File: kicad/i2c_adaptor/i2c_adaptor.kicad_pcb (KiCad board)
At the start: 2 copper layers, 12 parts, among them J2 Conn_01x05, J4 Conn_01x14, J5 Conn_01x02, J6 Conn_01x14, SW1 SW_SPDT, U1 pic16f1825

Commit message: update
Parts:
- moved R1 10.2 mm to (171.4, 128.3)
- moved C1 10.2 mm to (165.1, 121.9)
- moved U1 10.2 mm to (175.3, 121.9)
- moved R2 6.48 mm to (171.4, 97.8), turned to 0 degrees
- moved R3 5.39 mm to (171.4, 100.3), turned to 0 degrees
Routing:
- net +3V3: track 177.8 -> 195.6 mm, vias 2 -> 1
- net Net-(J2-Pad5): track 7.62 -> 22.9 mm
- net Net-(J4-Pad3): track 38.1 -> 48.3 mm
- net Net-(J4-Pad10): track 33.0 -> 43.2 mm
- net Net-(J2-Pad4): track 12.7 -> 22.9 mm
- net GND: track 142.2 -> 132.1 mm, vias 0 -> 4

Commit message: update
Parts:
- removed D1: 1A, pic16f1:diode
- added Q1: Fairchild BS170, pic16f1:BS170, F.Cu at (182.9, 110.5)
- moved J5 2.54 mm to (205.7, 134.6)
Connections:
- J2 pad 2: GND -> FET
- J4 pad 1: GND -> FET
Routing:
- net GND: track 132.1 -> 71.1 mm, vias 4 -> 2
- net FET: track 0.00 -> 50.8 mm, vias 0 -> 2
- net +3V3: track 195.6 -> 167.6 mm, vias 1 -> 2
- net Net-(Q1-Pad2): track 0.00 -> 7.62 mm
- net Net-(J4-Pad3): track 48.3 -> 53.3 mm
- net Net-(J4-Pad10): track 43.2 -> 48.3 mm
- net Net-(F1-Pad1): track 5.08 -> 7.62 mm

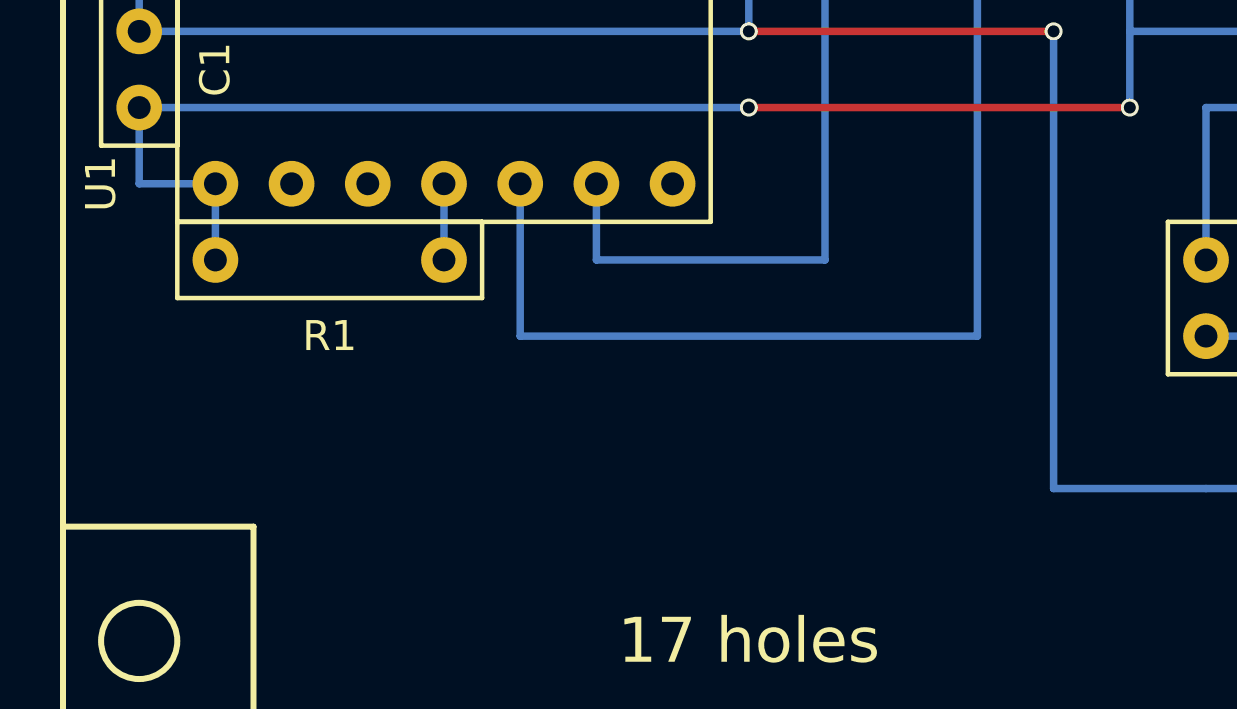
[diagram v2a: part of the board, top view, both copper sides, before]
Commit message: migration from PIC16F1825 to PIC16F18326
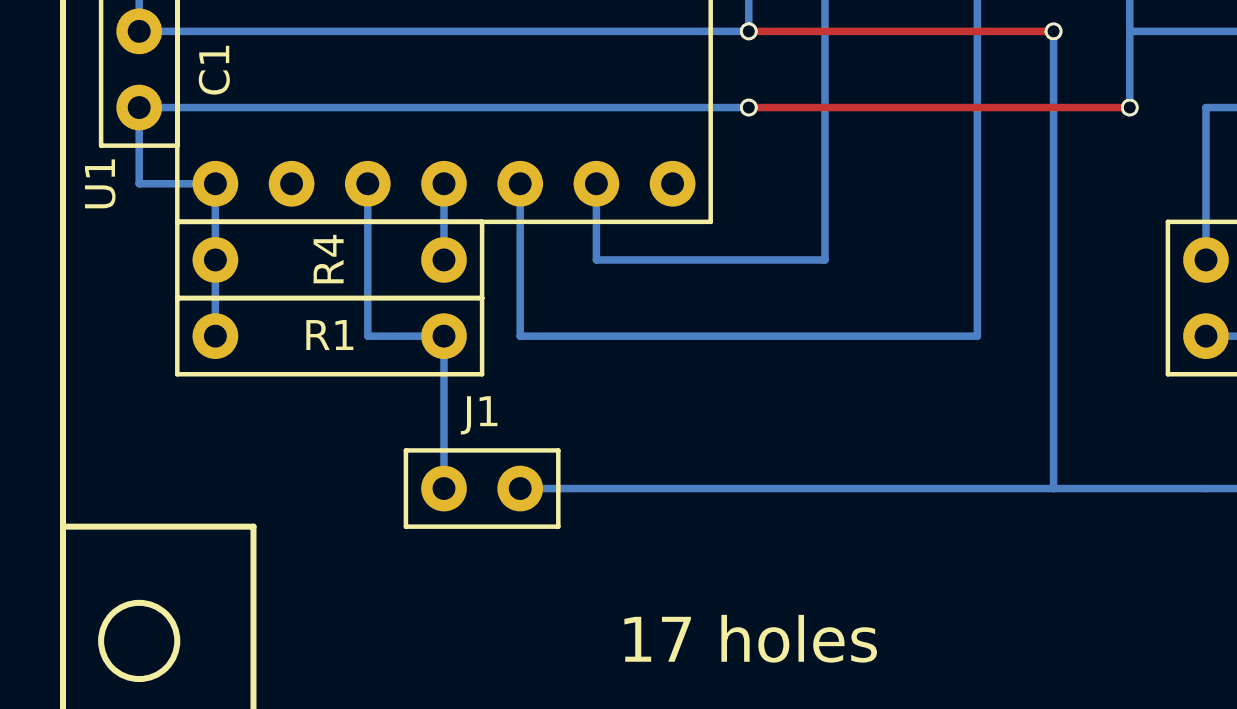
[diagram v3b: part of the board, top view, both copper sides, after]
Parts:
- added J1: Conn_01x02, mcu:Pin Header 2P, F.Cu at (176.5, 135.9)
- added R4: 51k, pic16f1:Register, F.Cu at (171.4, 130.8)
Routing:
- net GND: track 71.1 -> 88.9 mm
- net Net-(J1-Pad2): track 0.00 -> 12.7 mm
- net +3V3: track 167.6 -> 170.2 mm
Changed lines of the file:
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@@
 (kicad_pcb (version 4) (host pcbnew 4.0.7)
   (general
-    (links 26)
+    (links 30)
     (no_connects 0)
     (area 0 0 0 0)
     (thickness 1.6)
     (drawings 19)
-    (tracks 68)
+    (tracks 73)
     (zones 0)
-    (modules 12)
+    (modules 14)
     (nets 40)
   )
@@
   (net 32 "Net-(U1-Pad2)")
   (net 33 "Net-(U1-Pad13)")
-  (net 34 "Net-(U1-Pad3)")
-  (net 35 "Net-(U1-Pad12)")
-  (net 36 "Net-(U1-Pad11)")
-  (net 37 "Net-(U1-Pad7)")
-  (net 38 FET)
-  (net 39 "Net-(Q1-Pad2)")
+  (net 34 "Net-(U1-Pad12)")
+  (net 35 "Net-(U1-Pad11)")
+  (net 36 "Net-(U1-Pad7)")
+  (net 37 FET)
+  (net 38 "Net-(Q1-Pad2)")
+  (net 39 "Net-(J1-Pad2)")
   (net_class Default "This is the default net class."
     (clearance 0.2)
@@
     (add_net "Net-(F1-Pad1)")
     (add_net "Net-(F1-Pad2)")
+    (add_net "Net-(J1-Pad2)")
     (add_net "Net-(J2-Pad3)")
     (add_net "Net-(J2-Pad4)")
@@
     (add_net "Net-(U1-Pad13)")
     (add_net "Net-(U1-Pad2)")
-    (add_net "Net-(U1-Pad3)")
     (add_net "Net-(U1-Pad7)")
   )
@@
       (net 1 +3V3))
     (pad 2 thru_hole circle (at -2.54 0) (size 1.524 1.524) (drill 0.762) (layers *.Cu *.Mask)
-      (net 38 FET))
+      (net 37 FET))
     (pad 3 thru_hole circle (at 0 0) (size 1.524 1.524) (drill 0.762) (layers *.Cu *.Mask)
       (net 5 "Net-(J2-Pad3)"))
@@
     (fp_line (start -17.78 -1.27) (end -17.78 1.27) (layer F.SilkS) (width 0.15))
     (pad 1 thru_hole circle (at -16.51 0 270) (size 1.524 1.524) (drill 0.762) (layers *.Cu *.Mask)
-      (net 38 FET))
+      (net 37 FET))
     (pad 2 thru_hole circle (at -13.97 0 270) (size 1.524 1.524) (drill 0.762) (layers *.Cu *.Mask)
       (net 8 "Net-(J4-Pad2)"))
@@
       (net 33 "Net-(U1-Pad13)"))
     (pad 3 thru_hole circle (at -3.81 -2.54 90) (size 1.524 1.524) (drill 0.762) (layers *.Cu *.Mask)
-      (net 34 "Net-(U1-Pad3)"))
+      (net 39 "Net-(J1-Pad2)"))
     (pad 12 thru_hole circle (at 3.81 -2.54 90) (size 1.524 1.524) (drill 0.762) (layers *.Cu *.Mask)
-      (net 35 "Net-(U1-Pad12)"))
+      (net 34 "Net-(U1-Pad12)"))
     (pad 4 thru_hole circle (at -3.81 0 90) (size 1.524 1.524) (drill 0.762) (layers *.Cu *.Mask)
       (net 30 "Net-(R1-Pad1)"))
     (pad 11 thru_hole circle (at 3.81 0 90) (size 1.524 1.524) (drill 0.762) (layers *.Cu *.Mask)
-      (net 36 "Net-(U1-Pad11)"))
+      (net 35 "Net-(U1-Pad11)"))
     (pad 5 thru_hole circle (at -3.81 2.54 90) (size 1.524 1.524) (drill 0.762) (layers *.Cu *.Mask)
       (net 16 "Net-(J4-Pad10)"))
@@
       (net 6 "Net-(J2-Pad4)"))
     (pad 7 thru_hole circle (at -3.81 7.62 90) (size 1.524 1.524) (drill 0.762) (layers *.Cu *.Mask)
-      (net 37 "Net-(U1-Pad7)"))
+      (net 36 "Net-(U1-Pad7)"))
     (pad 8 thru_hole circle (at 3.81 7.62 90) (size 1.524 1.524) (drill 0.762) (layers *.Cu *.Mask)
-      (net 39 "Net-(Q1-Pad2)"))
+      (net 38 "Net-(Q1-Pad2)"))
   )
   (module pic16f1:Register (layer F.Cu)
@@
     (fp_line (start 3.81 -1.27) (end -3.81 -1.27) (layer F.SilkS) (width 0.15))
     (pad 1 thru_hole circle (at -2.54 0) (size 1.524 1.524) (drill 0.762) (layers *.Cu *.Mask)
-      (net 38 FET))
+      (net 37 FET))
     (pad 2 thru_hole circle (at 0 0) (size 1.524 1.524) (drill 0.762) (layers *.Cu *.Mask)
-      (net 39 "Net-(Q1-Pad2)"))
+      (net 38 "Net-(Q1-Pad2)"))
     (pad 3 thru_hole circle (at 2.54 0) (size 1.524 1.524) (drill 0.762) (layers *.Cu *.Mask)
       (net 2 GND))
+  )
+  (module "mcu:Pin Header 2P" (layer F.Cu)
+    (at 176.53 135.89 180)
+    (fp_text reference J1 (at 0 2.54 180) (layer F.SilkS)
+      (effects (font (size 1 1) (thickness 0.15)))
+    )
+    (fp_text value Conn_01x02 (at 0 -2.54 180) (layer F.Fab)
+      (effects (font (size 1 1) (thickness 0.15)))
+    )
+    (fp_line (start -2.54 -1.27) (end -2.54 1.27) (layer F.SilkS) (width 0.15))
+    (fp_line (start -2.54 1.27) (end 2.54 1.27) (layer F.SilkS) (width 0.15))
+    (fp_line (start 2.54 1.27) (end 2.54 -1.27) (layer F.SilkS) (width 0.15))
+    (fp_line (start 2.54 -1.27) (end -2.54 -1.27) (layer F.SilkS) (width 0.15))
+    (pad 1 thru_hole circle (at -1.27 0 180) (size 1.524 1.524) (drill 0.762) (layers *.Cu *.Mask)
+      (net 2 GND))
+    (pad 2 thru_hole circle (at 1.27 0 180) (size 1.524 1.524) (drill 0.762) (layers *.Cu *.Mask)
+      (net 39 "Net-(J1-Pad2)"))
+  )
+  (module pic16f1:Register (layer F.Cu)
+    (at 171.45 130.81)
+    (fp_text reference R4 (at 0 -2.54 90) (layer F.SilkS)
+      (effects (font (size 1 1) (thickness 0.15)))
+    )
+    (fp_text value 51k (at 0 2.54) (layer F.Fab)
+      (effects (font (size 1 1) (thickness 0.15)))
+    )
+    (fp_line (start -5.08 -1.27) (end 5.08 -1.27) (layer F.SilkS) (width 0.15))
+    (fp_line (start -5.08 -1.27) (end -5.08 1.27) (layer F.SilkS) (width 0.15))
+    (fp_line (start -5.08 1.27) (end 5.08 1.27) (layer F.SilkS) (width 0.15))
+    (fp_line (start 5.08 1.27) (end 5.08 -1.27) (layer F.SilkS) (width 0.15))
+    (pad 1 thru_hole circle (at -3.81 0) (size 1.524 1.524) (drill 0.762) (layers *.Cu *.Mask)
+      (net 1 +3V3))
+    (pad 2 thru_hole circle (at 3.81 0) (size 1.524 1.524) (drill 0.762) (layers *.Cu *.Mask)
+      (net 39 "Net-(J1-Pad2)"))
   )
   (gr_line (start 208.28 143.51) (end 162.56 143.51) (angle 90) (layer F.SilkS) (width 0.2))
@@
   (gr_line (start 208.28 72.39) (end 162.56 72.39) (angle 90) (layer F.SilkS) (width 0.2))
   (segment (start 185.42 99.06) (end 185.42 99.06) (width 0.25) (layer B.Cu) (net 0))
+  (segment (start 167.64 130.81) (end 167.64 128.27) (width 0.25) (layer B.Cu) (net 1))
   (segment (start 185.42 123.19) (end 198.12 123.19) (width 0.25) (layer F.Cu) (net 1))
   (segment (start 165.1 123.19) (end 185.42 123.19) (width 0.25) (layer B.Cu) (net 1))
@@
   (segment (start 167.64 102.87) (end 167.64 100.33) (width 0.25) (layer B.Cu) (net 1))
   (segment (start 167.64 128.27) (end 167.64 125.73) (width 0.25) (layer B.Cu) (net 1) (status 10))
+  (segment (start 177.8 135.89) (end 195.58 135.89) (width 0.25) (layer B.Cu) (net 2) (status 400000))
   (segment (start 185.42 120.65) (end 195.58 120.65) (width 0.25) (layer F.Cu) (net 2))
   (segment (start 185.42 120.65) (end 185.42 110.49) (width 0.25) (layer B.Cu) (net 2) (status 20))
@@
   (segment (start 193.04 105.41) (end 190.5 105.41) (width 0.25) (layer B.Cu) (net 16))
   (segment (start 175.26 128.27) (end 175.26 125.73) (width 0.25) (layer B.Cu) (net 30) (status 10))
-  (segment (start 182.88 82.55) (end 180.34 82.55) (width 0.25) (layer B.Cu) (net 38))
-  (segment (start 190.5 82.55) (end 182.88 82.55) (width 0.25) (layer B.Cu) (net 38))
-  (segment (start 180.34 82.55) (end 180.34 105.41) (width 0.25) (layer B.Cu) (net 38))
-  (segment (start 170.18 102.87) (end 170.18 105.41) (width 0.25) (layer B.Cu) (net 38))
-  (via (at 180.34 105.41) (size 0.6) (drill 0.4) (layers F.Cu B.Cu) (net 38))
-  (segment (start 172.72 105.41) (end 180.34 105.41) (width 0.25) (layer F.Cu) (net 38))
-  (via (at 172.72 105.41) (size 0.6) (drill 0.4) (layers F.Cu B.Cu) (net 38))
-  (segment (start 170.18 105.41) (end 172.72 105.41) (width 0.25) (layer B.Cu) (net 38))
-  (segment (start 180.34 110.49) (end 180.34 105.41) (width 0.25) (layer B.Cu) (net 38) (status 10))
-  (segment (start 182.88 118.11) (end 182.88 110.49) (width 0.25) (layer B.Cu) (net 39))
-  (segment (start 182.88 110.49) (end 182.88 110.49) (width 0.25) (layer B.Cu) (net 39) (status 20))
+  (segment (start 182.88 82.55) (end 180.34 82.55) (width 0.25) (layer B.Cu) (net 37))
+  (segment (start 190.5 82.55) (end 182.88 82.55) (width 0.25) (layer B.Cu) (net 37))
+  (segment (start 180.34 82.55) (end 180.34 105.41) (width 0.25) (layer B.Cu) (net 37))
+  (segment (start 170.18 102.87) (end 170.18 105.41) (width 0.25) (layer B.Cu) (net 37))
+  (via (at 180.34 105.41) (size 0.6) (drill 0.4) (layers F.Cu B.Cu) (net 37))
+  (segment (start 172.72 105.41) (end 180.34 105.41) (width 0.25) (layer F.Cu) (net 37))
+  (via (at 172.72 105.41) (size 0.6) (drill 0.4) (layers F.Cu B.Cu) (net 37))
+  (segment (start 170.18 105.41) (end 172.72 105.41) (width 0.25) (layer B.Cu) (net 37))
+  (segment (start 180.34 110.49) (end 180.34 105.41) (width 0.25) (layer B.Cu) (net 37) (status 10))
+  (segment (start 182.88 118.11) (end 182.88 110.49) (width 0.25) (layer B.Cu) (net 38))
+  (segment (start 182.88 110.49) (end 182.88 110.49) (width 0.25) (layer B.Cu) (net 38) (status 20))
+  (segment (start 175.26 130.81) (end 175.26 135.89) (width 0.25) (layer B.Cu) (net 39) (status C00000))
+  (segment (start 172.72 125.73) (end 172.72 130.81) (width 0.25) (layer B.Cu) (net 39) (status 400000))
+  (segment (start 172.72 130.81) (end 175.26 130.81) (width 0.25) (layer B.Cu) (net 39) (status 800000))
 )

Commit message: update
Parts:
- added D1: 1A, pic16f1:diode, F.Cu at (198.1, 130.8)
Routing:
- net +3V3: track 170.2 -> 174.0 mm
- net GND: track 88.9 -> 90.2 mm
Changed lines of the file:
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@@
 (kicad_pcb (version 4) (host pcbnew 4.0.7)
   (general
-    (links 30)
+    (links 32)
     (no_connects 0)
     (area 0 0 0 0)
     (thickness 1.6)
     (drawings 19)
-    (tracks 73)
+    (tracks 76)
     (zones 0)
-    (modules 14)
+    (modules 15)
     (nets 40)
   )
@@
       (net 39 "Net-(J1-Pad2)"))
   )
+  (module pic16f1:diode (layer F.Cu)
+    (at 198.12 130.81 270)
+    (fp_text reference D1 (at 0 2.54 270) (layer F.SilkS)
+      (effects (font (size 1 1) (thickness 0.15)))
+    )
+    (fp_text value 1A (at 0 -2.54 270) (layer F.Fab)
+      (effects (font (size 1 1) (thickness 0.15)))
+    )
+    (fp_line (start -5.08 -1.27) (end -5.08 1.27) (layer F.SilkS) (width 0.15))
+    (fp_line (start -5.08 1.27) (end 5.08 1.27) (layer F.SilkS) (width 0.15))
+    (fp_line (start 5.08 1.27) (end 5.08 -1.27) (layer F.SilkS) (width 0.15))
+    (fp_line (start 5.08 -1.27) (end -5.08 -1.27) (layer F.SilkS) (width 0.15))
+    (pad 1 thru_hole circle (at -3.81 0 270) (size 1.524 1.524) (drill 0.762) (layers *.Cu *.Mask)
+      (net 1 +3V3))
+    (pad 2 thru_hole circle (at 3.81 0 270) (size 1.524 1.524) (drill 0.762) (layers *.Cu *.Mask)
+      (net 2 GND))
+  )
   (gr_line (start 208.28 143.51) (end 162.56 143.51) (angle 90) (layer F.SilkS) (width 0.2))
   (gr_line (start 208.28 72.39) (end 208.28 143.51) (angle 90) (layer F.SilkS) (width 0.2))
@@
   (gr_line (start 208.28 72.39) (end 162.56 72.39) (angle 90) (layer F.SilkS) (width 0.2))
   (segment (start 185.42 99.06) (end 185.42 99.06) (width 0.25) (layer B.Cu) (net 0))
+  (segment (start 198.12 127) (end 198.12 123.19) (width 0.25) (layer B.Cu) (net 1) (status 400000))
   (segment (start 167.64 130.81) (end 167.64 128.27) (width 0.25) (layer B.Cu) (net 1))
   (segment (start 185.42 123.19) (end 198.12 123.19) (width 0.25) (layer F.Cu) (net 1))
@@
   (segment (start 167.64 102.87) (end 167.64 100.33) (width 0.25) (layer B.Cu) (net 1))
   (segment (start 167.64 128.27) (end 167.64 125.73) (width 0.25) (layer B.Cu) (net 1) (status 10))
-  (segment (start 177.8 135.89) (end 195.58 135.89) (width 0.25) (layer B.Cu) (net 2) (status 400000))
+  (segment (start 198.12 134.62) (end 198.12 135.89) (width 0.25) (layer B.Cu) (net 2) (status 400000))
+  (segment (start 177.8 135.89) (end 195.58 135.89) (width 0.25) (layer B.Cu) (net 2))
   (segment (start 185.42 120.65) (end 195.58 120.65) (width 0.25) (layer F.Cu) (net 2))
   (segment (start 185.42 120.65) (end 185.42 110.49) (width 0.25) (layer B.Cu) (net 2) (status 20))
-  (segment (start 200.66 135.89) (end 195.58 135.89) (width 0.25) (layer B.Cu) (net 2))
+  (segment (start 200.66 135.89) (end 198.12 135.89) (width 0.25) (layer B.Cu) (net 2))
+  (segment (start 198.12 135.89) (end 195.58 135.89) (width 0.25) (layer B.Cu) (net 2))
   (segment (start 195.58 135.89) (end 195.58 120.65) (width 0.25) (layer B.Cu) (net 2))
   (segment (start 200.66 135.89) (end 205.74 135.89) (width 0.25) (layer B.Cu) (net 2) (status 20))
@@
   (segment (start 182.88 118.11) (end 182.88 110.49) (width 0.25) (layer B.Cu) (net 38))
   (segment (start 182.88 110.49) (end 182.88 110.49) (width 0.25) (layer B.Cu) (net 38) (status 20))
-  (segment (start 175.26 130.81) (end 175.26 135.89) (width 0.25) (layer B.Cu) (net 39) (status C00000))
-  (segment (start 172.72 125.73) (end 172.72 130.81) (width 0.25) (layer B.Cu) (net 39) (status 400000))
-  (segment (start 172.72 130.81) (end 175.26 130.81) (width 0.25) (layer B.Cu) (net 39) (status 800000))
+  (segment (start 175.26 130.81) (end 175.26 135.89) (width 0.25) (layer B.Cu) (net 39))
+  (segment (start 172.72 125.73) (end 172.72 130.81) (width 0.25) (layer B.Cu) (net 39))
+  (segment (start 172.72 130.81) (end 175.26 130.81) (width 0.25) (layer B.Cu) (net 39))
 )
